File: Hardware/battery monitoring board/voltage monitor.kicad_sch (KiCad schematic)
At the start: 16 parts, among them J1 S5B-XH-A

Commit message: erc-clear battery board
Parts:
- J1: footprint S5B-XH-A:JST_S5B-XH-A -> Connector_JST:JST_XH_B5B-XH-A_1x05_P2.50mm_Vertical
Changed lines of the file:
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@@
         )
         (path "/bf623d80-ca5a-491f-9daa-4dffbeba5279/986cc9e1-c37e-4aa2-b3b5-8e2dcbe750c5"
-          (reference "TP2") (unit 1)
-        )
-        (path "/bf623d80-ca5a-491f-9daa-4dffbeba5279/26c6129c-8fb5-4658-8c7a-1dc4298981ba"
-          (reference "TP16") (unit 1)
+          (reference "2") (unit 1)
+        )
+        (path "/bf623d80-ca5a-491f-9daa-4dffbeba5279/26c6129c-8fb5-4658-8c7a-1dc4298981ba"
+          (reference "2") (unit 1)
         )
       )
@@
         )
         (path "/bf623d80-ca5a-491f-9daa-4dffbeba5279/986cc9e1-c37e-4aa2-b3b5-8e2dcbe750c5"
-          (reference "TP1") (unit 1)
-        )
-        (path "/bf623d80-ca5a-491f-9daa-4dffbeba5279/26c6129c-8fb5-4658-8c7a-1dc4298981ba"
-          (reference "TP15") (unit 1)
+          (reference "1") (unit 1)
+        )
+        (path "/bf623d80-ca5a-491f-9daa-4dffbeba5279/26c6129c-8fb5-4658-8c7a-1dc4298981ba"
+          (reference "1") (unit 1)
         )
       )
@@
       (effects (font (size 1.27 1.27)))
     )
-    (property "Footprint" "S5B-XH-A:JST_S5B-XH-A" (at 26.67 31.75 0)
+    (property "Footprint" "Connector_JST:JST_XH_B5B-XH-A_1x05_P2.50mm_Vertical" (at 26.67 31.75 0)
       (effects (font (size 1.27 1.27)) (justify bottom) hide)
     )
@@
         )
         (path "/bf623d80-ca5a-491f-9daa-4dffbeba5279/986cc9e1-c37e-4aa2-b3b5-8e2dcbe750c5"
-          (reference "J3") (unit 1)
-        )
-        (path "/bf623d80-ca5a-491f-9daa-4dffbeba5279/26c6129c-8fb5-4658-8c7a-1dc4298981ba"
-          (reference "J10") (unit 1)
+          (reference "J3 -") (unit 1)
+        )
+        (path "/bf623d80-ca5a-491f-9daa-4dffbeba5279/26c6129c-8fb5-4658-8c7a-1dc4298981ba"
+          (reference "J9 +") (unit 1)
         )
       )
@@
         )
         (path "/bf623d80-ca5a-491f-9daa-4dffbeba5279/986cc9e1-c37e-4aa2-b3b5-8e2dcbe750c5"
-          (reference "TP4") (unit 1)
-        )
-        (path "/bf623d80-ca5a-491f-9daa-4dffbeba5279/26c6129c-8fb5-4658-8c7a-1dc4298981ba"
-          (reference "TP18") (unit 1)
+          (reference "4") (unit 1)
+        )
+        (path "/bf623d80-ca5a-491f-9daa-4dffbeba5279/26c6129c-8fb5-4658-8c7a-1dc4298981ba"
+          (reference "4") (unit 1)
         )
       )
@@
         )
         (path "/bf623d80-ca5a-491f-9daa-4dffbeba5279/986cc9e1-c37e-4aa2-b3b5-8e2dcbe750c5"
-          (reference "TP3") (unit 1)
-        )
-        (path "/bf623d80-ca5a-491f-9daa-4dffbeba5279/26c6129c-8fb5-4658-8c7a-1dc4298981ba"
-          (reference "TP17") (unit 1)
-        )
-      )
+          (reference "3") (unit 1)
+        )
+        (path "/bf623d80-ca5a-491f-9daa-4dffbeba5279/26c6129c-8fb5-4658-8c7a-1dc4298981ba"
+          (reference "3") (unit 1)
+        )
+      )

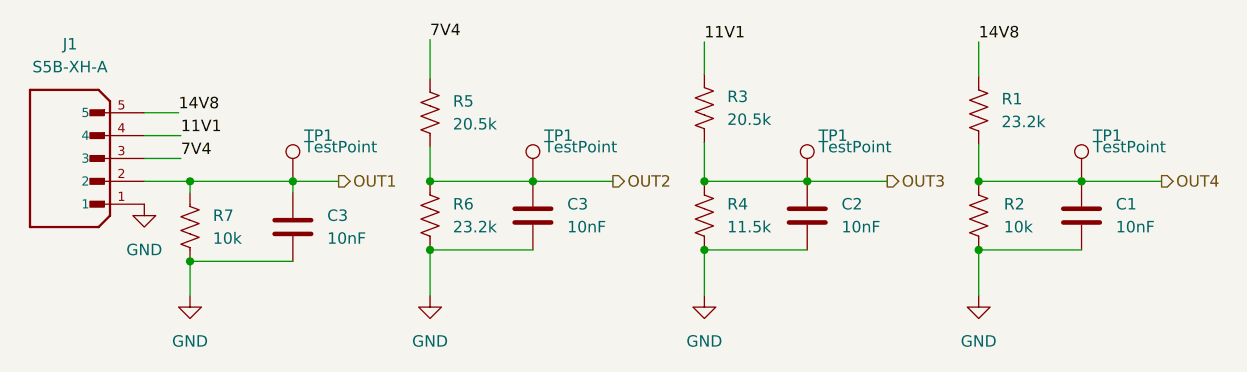
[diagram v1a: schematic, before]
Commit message: updated battery pcb (voltage dividers etc)
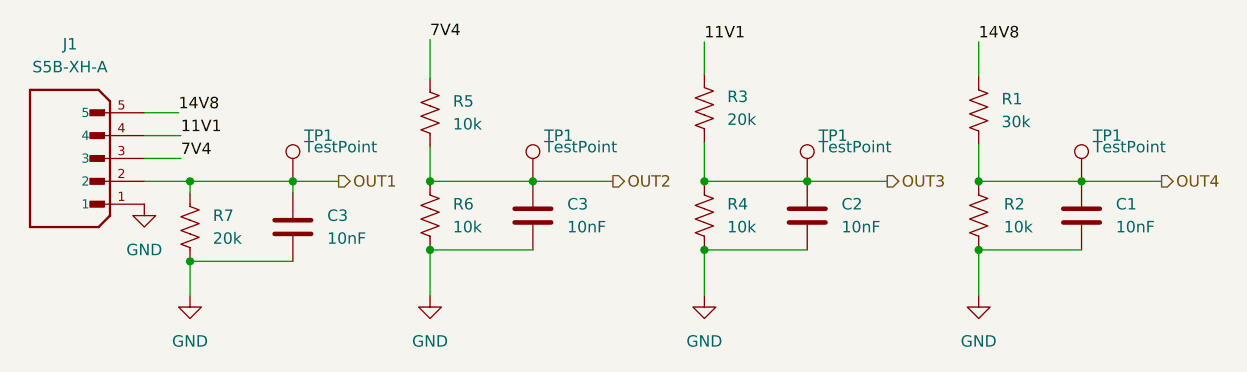
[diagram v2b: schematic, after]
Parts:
- R1: value 23.2k -> 30k
- R3: value 20.5k -> 20k
- R4: value 11.5k -> 10k
- R5: value 20.5k -> 10k
- R6: value 23.2k -> 10k
- R7: value 10k -> 20k
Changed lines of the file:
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@@
       (effects (font (size 1.27 1.27)) (justify left))
     )
-    (property "Value" "10k" (at 39.37 40.64 0)
+    (property "Value" "20k" (at 39.37 40.64 0)
       (effects (font (size 1.27 1.27)) (justify left))
     )
@@
       (effects (font (size 1.27 1.27)) (justify left))
     )
-    (property "Value" "11.5k" (at 96.52 39.37 0)
+    (property "Value" "10k" (at 96.52 39.37 0)
       (effects (font (size 1.27 1.27)) (justify left))
     )
@@
         )
         (path "/bf623d80-ca5a-491f-9daa-4dffbeba5279/986cc9e1-c37e-4aa2-b3b5-8e2dcbe750c5"
-          (reference "2") (unit 1)
+          (reference "21") (unit 1)
         )
         (path "/bf623d80-ca5a-491f-9daa-4dffbeba5279/26c6129c-8fb5-4658-8c7a-1dc4298981ba"
@@
       (effects (font (size 1.27 1.27)) (justify right))
     )
-    (property "Value" "20.5k" (at 96.52 27.432 0)
+    (property "Value" "20k" (at 96.52 27.432 0)
       (effects (font (size 1.27 1.27)) (justify right))
     )
@@
         )
         (path "/bf623d80-ca5a-491f-9daa-4dffbeba5279/986cc9e1-c37e-4aa2-b3b5-8e2dcbe750c5"
-          (reference "1") (unit 1)
-        )
-        (path "/bf623d80-ca5a-491f-9daa-4dffbeba5279/26c6129c-8fb5-4658-8c7a-1dc4298981ba"
-          (reference "1") (unit 1)
+          (reference "11") (unit 1)
+        )
+        (path "/bf623d80-ca5a-491f-9daa-4dffbeba5279/26c6129c-8fb5-4658-8c7a-1dc4298981ba"
+          (reference "12") (unit 1)
         )
       )
@@
       (effects (font (size 1.27 1.27)) (justify right))
     )
-    (property "Value" "23.2k" (at 127 27.686 0)
+    (property "Value" "30k" (at 127 27.686 0)
       (effects (font (size 1.27 1.27)) (justify right))
     )
@@
       (effects (font (size 1.27 1.27)) (justify left))
     )
-    (property "Value" "23.2k" (at 66.04 39.37 0)
+    (property "Value" "10k" (at 66.04 39.37 0)
       (effects (font (size 1.27 1.27)) (justify left))
     )
@@
       (effects (font (size 1.27 1.27)) (justify right))
     )
-    (property "Value" "20.5k" (at 66.04 27.94 0)
+    (property "Value" "10k" (at 66.04 27.94 0)
       (effects (font (size 1.27 1.27)) (justify right))
     )
@@
         )
         (path "/bf623d80-ca5a-491f-9daa-4dffbeba5279/986cc9e1-c37e-4aa2-b3b5-8e2dcbe750c5"
-          (reference "J3 -") (unit 1)
-        )
-        (path "/bf623d80-ca5a-491f-9daa-4dffbeba5279/26c6129c-8fb5-4658-8c7a-1dc4298981ba"
-          (reference "J9 +") (unit 1)
+          (reference "J3 -1") (unit 1)
+        )
+        (path "/bf623d80-ca5a-491f-9daa-4dffbeba5279/26c6129c-8fb5-4658-8c7a-1dc4298981ba"
+          (reference "J9 +1") (unit 1)
         )
       )
@@
         )
         (path "/bf623d80-ca5a-491f-9daa-4dffbeba5279/986cc9e1-c37e-4aa2-b3b5-8e2dcbe750c5"
-          (reference "4") (unit 1)
-        )
-        (path "/bf623d80-ca5a-491f-9daa-4dffbeba5279/26c6129c-8fb5-4658-8c7a-1dc4298981ba"
-          (reference "4") (unit 1)
+          (reference "41") (unit 1)
+        )
+        (path "/bf623d80-ca5a-491f-9daa-4dffbeba5279/26c6129c-8fb5-4658-8c7a-1dc4298981ba"
+          (reference "42") (unit 1)
         )
       )
@@
         )
         (path "/bf623d80-ca5a-491f-9daa-4dffbeba5279/986cc9e1-c37e-4aa2-b3b5-8e2dcbe750c5"
-          (reference "3") (unit 1)
-        )
-        (path "/bf623d80-ca5a-491f-9daa-4dffbeba5279/26c6129c-8fb5-4658-8c7a-1dc4298981ba"
-          (reference "3") (unit 1)
-        )
-      )
+          (reference "31") (unit 1)
+        )
+        (path "/bf623d80-ca5a-491f-9daa-4dffbeba5279/26c6129c-8fb5-4658-8c7a-1dc4298981ba"
+          (reference "32") (unit 1)
+        )
+      )

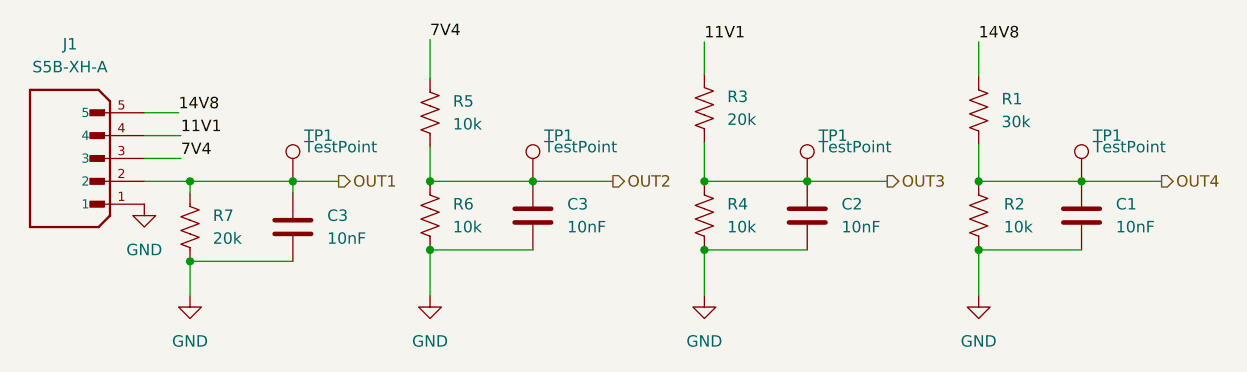
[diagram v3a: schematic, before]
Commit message: resolved erc/drc issues
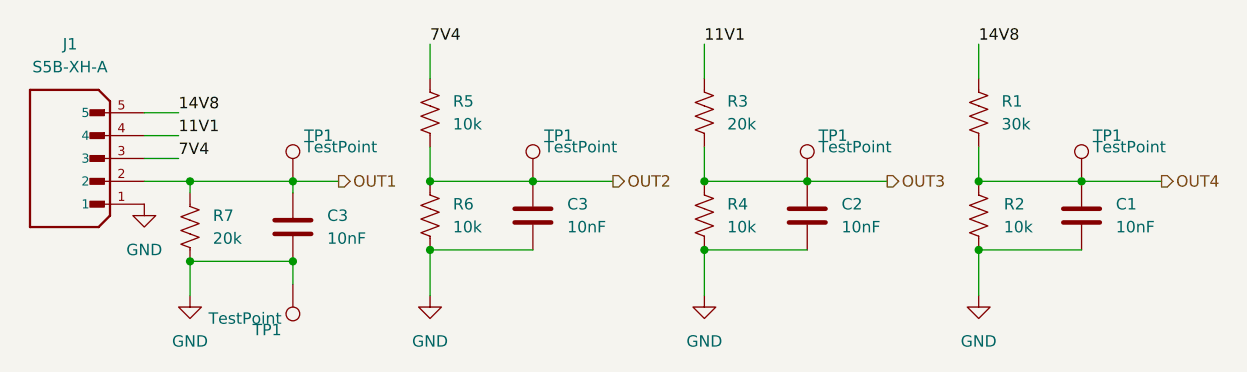
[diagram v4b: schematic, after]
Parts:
- added TP1: TestPoint, PCM_4ms_TestPoint:TestPoint_Pad_06, symbol Connector:TestPoint
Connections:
- net GND: now also TP1.1
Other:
- moved on the sheet: R3
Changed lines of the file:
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@@
   (junction (at 93.98 34.29) (diameter 0) (color 0 0 0 0)
   )
+  (junction (at 48.26 43.18) (diameter 0) (color 0 0 0 0)
+  )
   (junction (at 135.89 34.29) (diameter 0) (color 0 0 0 0)
   )
@@
     (stroke (width 0) (type default))
   )
-  (wire (pts (xy 31.75 31.75) (xy 35.814 31.75))
+  (wire (pts (xy 31.75 31.75) (xy 35.56 31.75))
+    (stroke (width 0) (type default))
+  )
+  (wire (pts (xy 48.26 43.18) (xy 48.26 45.72))
     (stroke (width 0) (type default))
   )
@@
     (stroke (width 0) (type default))
   )
-  (wire (pts (xy 31.75 29.21) (xy 35.814 29.21))
+  (wire (pts (xy 31.75 29.21) (xy 35.56 29.21))
     (stroke (width 0) (type default))
   )
@@
     (stroke (width 0) (type default))
   )
-  (wire (pts (xy 124.46 18.796) (xy 124.46 22.606))
+  (wire (pts (xy 124.46 19.05) (xy 124.46 22.86))
     (stroke (width 0) (type default))
   )
@@
     (stroke (width 0) (type default))
   )
-  (wire (pts (xy 93.98 29.972) (xy 93.98 34.29))
+  (wire (pts (xy 93.98 30.48) (xy 93.98 34.29))
     (stroke (width 0) (type default))
   )
@@
     (stroke (width 0) (type default))
   )
-  (wire (pts (xy 63.5 18.542) (xy 63.5 22.86))
+  (wire (pts (xy 63.5 19.05) (xy 63.5 22.86))
     (stroke (width 0) (type default))
   )
@@
     (stroke (width 0) (type default))
   )
-  (wire (pts (xy 93.98 18.796) (xy 93.98 22.352))
-    (stroke (width 0) (type default))
-  )
-  (wire (pts (xy 124.46 30.226) (xy 124.46 34.29))
-    (stroke (width 0) (type default))
-  )
-  (label "7V4" (at 63.5 18.542 0) (fields_autoplaced)
+  (wire (pts (xy 93.98 19.05) (xy 93.98 22.86))
+    (stroke (width 0) (type default))
+  )
+  (wire (pts (xy 124.46 30.48) (xy 124.46 34.29))
+    (stroke (width 0) (type default))
+  )
+  (label "7V4" (at 63.5 19.05 0) (fields_autoplaced)
     (effects (font (size 1.27 1.27)) (justify left bottom))
   )
-  (label "11V1" (at 93.98 18.796 0) (fields_autoplaced)
+  (label "11V1" (at 93.98 19.05 0) (fields_autoplaced)
     (effects (font (size 1.27 1.27)) (justify left bottom))
   )
-  (label "7V4" (at 35.814 31.75 0) (fields_autoplaced)
+  (label "7V4" (at 35.56 31.75 0) (fields_autoplaced)
     (effects (font (size 1.27 1.27)) (justify left bottom))
   )
@@
     (effects (font (size 1.27 1.27)) (justify left bottom))
   )
-  (label "14V8" (at 124.46 18.796 0) (fields_autoplaced)
+  (label "14V8" (at 124.46 19.05 0) (fields_autoplaced)
     (effects (font (size 1.27 1.27)) (justify left bottom))
   )
-  (label "11V1" (at 35.814 29.21 0) (fields_autoplaced)
+  (label "11V1" (at 35.56 29.21 0) (fields_autoplaced)
     (effects (font (size 1.27 1.27)) (justify left bottom))
   )
@@
         (path "/bf623d80-ca5a-491f-9daa-4dffbeba5279/26c6129c-8fb5-4658-8c7a-1dc4298981ba"
           (reference "#PWR033") (unit 1)
+        )
+      )
+    )
+  )
+  (symbol (lib_id "Connector:TestPoint") (at 48.26 45.72 180) (unit 1)
+    (in_bom yes) (on_board yes) (dnp no)
+    (property "Reference" "TP1" (at 47.0041 50.8 0)
+      (effects (font (size 1.27 1.27)) (justify left))
+    )
+    (property "Value" "TestPoint" (at 47.0041 49.53 0)
+      (effects (font (size 1.27 1.27)) (justify left))
+    )
+    (property "Footprint" "PCM_4ms_TestPoint:TestPoint_Pad_06" (at 43.18 45.72 0)
+      (effects (font (size 1.27 1.27)) hide)
+    )
+    (property "Datasheet" "~" (at 43.18 45.72 0)
+      (effects (font (size 1.27 1.27)) hide)
+    )
+    (pin "1")
+    (instances
+      (project "battery monitoring board"
+        (path "/bf623d80-ca5a-491f-9daa-4dffbeba5279/5ec2dbdf-a276-4d4c-99fc-008475c1e770"
+          (reference "TP1") (unit 1)
+        )
+        (path "/bf623d80-ca5a-491f-9daa-4dffbeba5279/d1e89632-1041-42ed-815d-03472eda859a"
+          (reference "TP9") (unit 1)
+        )
+        (path "/bf623d80-ca5a-491f-9daa-4dffbeba5279/986cc9e1-c37e-4aa2-b3b5-8e2dcbe750c5"
+          (reference "ground1") (unit 1)
+        )
+        (path "/bf623d80-ca5a-491f-9daa-4dffbeba5279/26c6129c-8fb5-4658-8c7a-1dc4298981ba"
+          (reference "TP4") (unit 1)
         )
       )
@@
     )
   )
-  (symbol (lib_id "Device:R_US") (at 93.98 26.162 180) (unit 1)
-    (in_bom yes) (on_board yes) (dnp no) (fields_autoplaced)
-    (property "Reference" "R3" (at 96.52 24.892 0)
+  (symbol (lib_id "Device:R_US") (at 93.98 26.67 180) (unit 1)
+    (in_bom yes) (on_board yes) (dnp no) (fields_autoplaced)
+    (property "Reference" "R3" (at 96.52 25.4 0)
       (effects (font (size 1.27 1.27)) (justify right))
     )
-    (property "Value" "20k" (at 96.52 27.432 0)
+    (property "Value" "20k" (at 96.52 27.94 0)
       (effects (font (size 1.27 1.27)) (justify right))
     )
-    (property "Footprint" "Resistor_SMD:R_0805_2012Metric_Pad1.20x1.40mm_HandSolder" (at 92.964 25.908 90)
-      (effects (font (size 1.27 1.27)) hide)
-    )
-    (property "Datasheet" "~" (at 93.98 26.162 0)
+    (property "Footprint" "Resistor_SMD:R_0805_2012Metric_Pad1.20x1.40mm_HandSolder" (at 92.964 26.416 90)
+      (effects (font (size 1.27 1.27)) hide)
+    )
+    (property "Datasheet" "~" (at 93.98 26.67 0)
       (effects (font (size 1.27 1.27)) hide)
     )
@@
     )
   )
-  (symbol (lib_id "Device:R_US") (at 124.46 26.416 180) (unit 1)
-    (in_bom yes) (on_board yes) (dnp no) (fields_autoplaced)
-    (property "Reference" "R1" (at 127 25.146 0)
+  (symbol (lib_id "Device:R_US") (at 124.46 26.67 180) (unit 1)
+    (in_bom yes) (on_board yes) (dnp no) (fields_autoplaced)
+    (property "Reference" "R1" (at 127 25.4 0)
       (effects (font (size 1.27 1.27)) (justify right))
     )
-    (property "Value" "30k" (at 127 27.686 0)
+    (property "Value" "30k" (at 127 27.94 0)
       (effects (font (size 1.27 1.27)) (justify right))
     )
-    (property "Footprint" "Resistor_SMD:R_0805_2012Metric_Pad1.20x1.40mm_HandSolder" (at 123.444 26.162 90)
-      (effects (font (size 1.27 1.27)) hide)
-    )
-    (property "Datasheet" "~" (at 124.46 26.416 0)
+    (property "Footprint" "Resistor_SMD:R_0805_2012Metric_Pad1.20x1.40mm_HandSolder" (at 123.444 26.416 90)
+      (effects (font (size 1.27 1.27)) hide)
+    )
+    (property "Datasheet" "~" (at 124.46 26.67 0)
       (effects (font (size 1.27 1.27)) hide)
     )
@@
         )
         (path "/bf623d80-ca5a-491f-9daa-4dffbeba5279/986cc9e1-c37e-4aa2-b3b5-8e2dcbe750c5"
-          (reference "J3 -1") (unit 1)
-        )
-        (path "/bf623d80-ca5a-491f-9daa-4dffbeba5279/26c6129c-8fb5-4658-8c7a-1dc4298981ba"
-          (reference "J9 +1") (unit 1)
-        )
-      )
+          (reference "J3") (unit 1)
+        )
+        (path "/bf623d80-ca5a-491f-9daa-4dffbeba5279/26c6129c-8fb5-4658-8c7a-1dc4298981ba"
+          (reference "J9") (unit 1)
+        )
+      )
